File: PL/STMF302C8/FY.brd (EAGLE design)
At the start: 70 x 69 mm, 55 parts, among them J1 CON-SD-CARD_MICROSD-2908-05, J2 Flash Programming, U1 AS72652-BLGT, U2 AS72653-BLGT, U3 STM32F302C8T6, U4 AS72651-BLGT, U5 AMS1117-3.3, U6 4MB Flash, X1 JST-XH-04-PIN-LONG-PAD, Y2 ABM2B-8.000MHZ-10-1-U-T

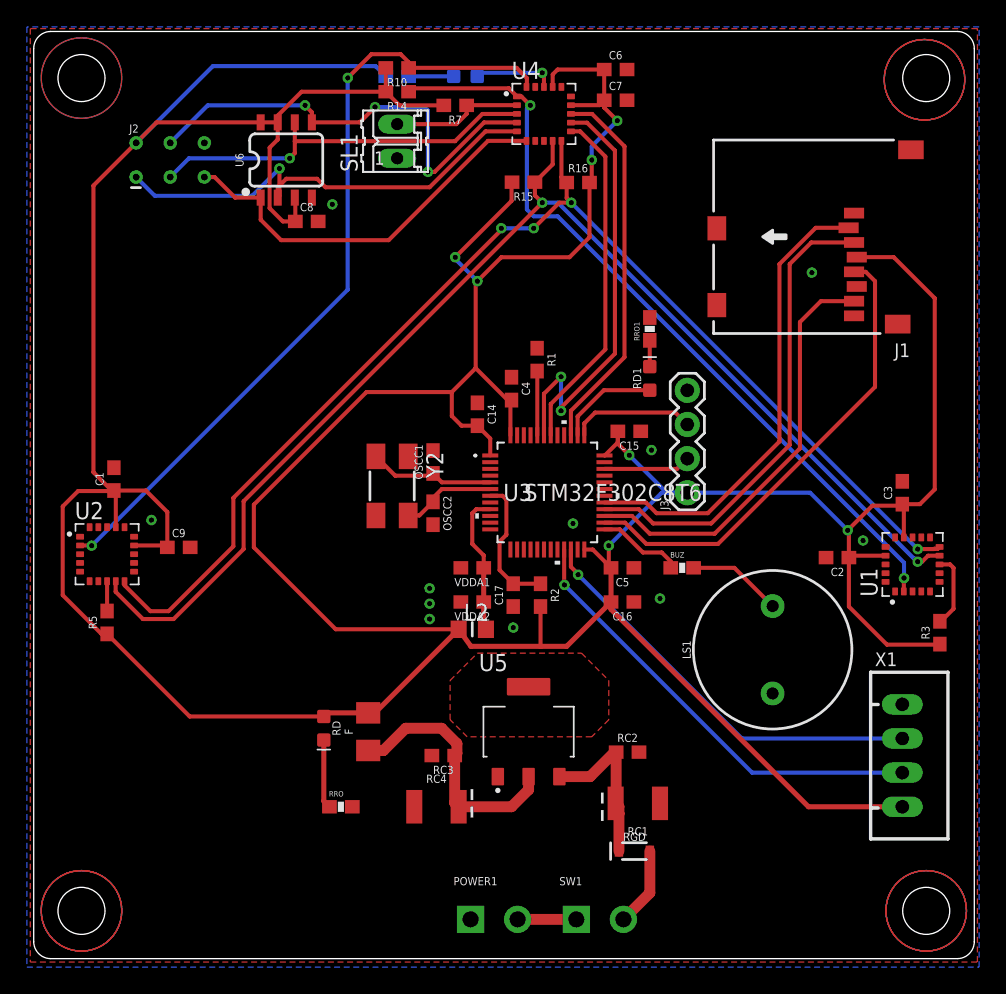
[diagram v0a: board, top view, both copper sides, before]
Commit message: Component name locations was arranged
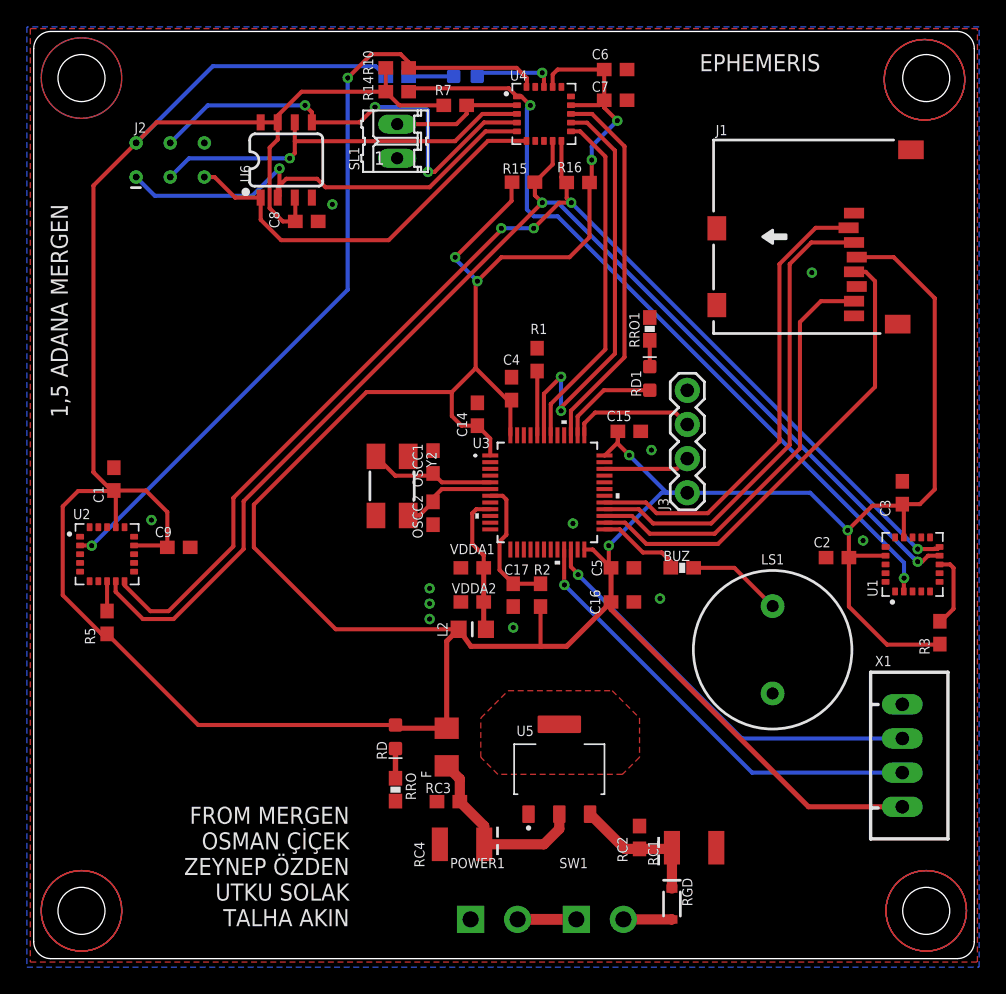
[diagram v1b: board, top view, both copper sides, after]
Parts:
- moved RC2 6.41 mm to (45.1, 9.02), turned to 90 degrees
- moved F 5.95 mm to (30.7, 15.7)
- moved RD 5.37 mm to (26.9, 16.5)
- moved RC1 5.34 mm to (49.1, 8.26)
- moved RGD 4.83 mm to (47.5, 4.06), turned to 270 degrees
- moved RRO 4.26 mm to (26.9, 12.6), turned to 270 degrees
- moved U5 3.61 mm to (39.1, 14.1)
- moved RC3 3.45 mm to (30.9, 11.7)
- moved RC4 3.38 mm to (31.9, 8.51)
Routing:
- net N$6: track 19.4 -> 14.2 mm
- net 3.3V: track 378.2 -> 382.7 mm
- net VNR: track 13.3 -> 10.2 mm
- net N$11: track 5.14 -> 2.21 mm
- net VIN: track 5.90 -> 3.61 mm
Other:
- board text added: "1,5 ADANA MERGEN"
- board text added: "EPHEMERIS"
- board text added: "FROM MERGEN OSMAN ÇİÇEK ZEYNEP ÖZDEN UTKU SOLAK TALHA AKIN"
